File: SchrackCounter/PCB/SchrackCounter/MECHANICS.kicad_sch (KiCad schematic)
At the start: 24 parts, among them J3 Conn_01x02_Pin, J4 Conn_01x02_Pin, J5 MEM2067-02-180-00-A_REVB, M1 Fan_CPU_4pin, SW1 SW_Push, SW2 SW_Push, SW3 SW_Push, SW4 SW_Push

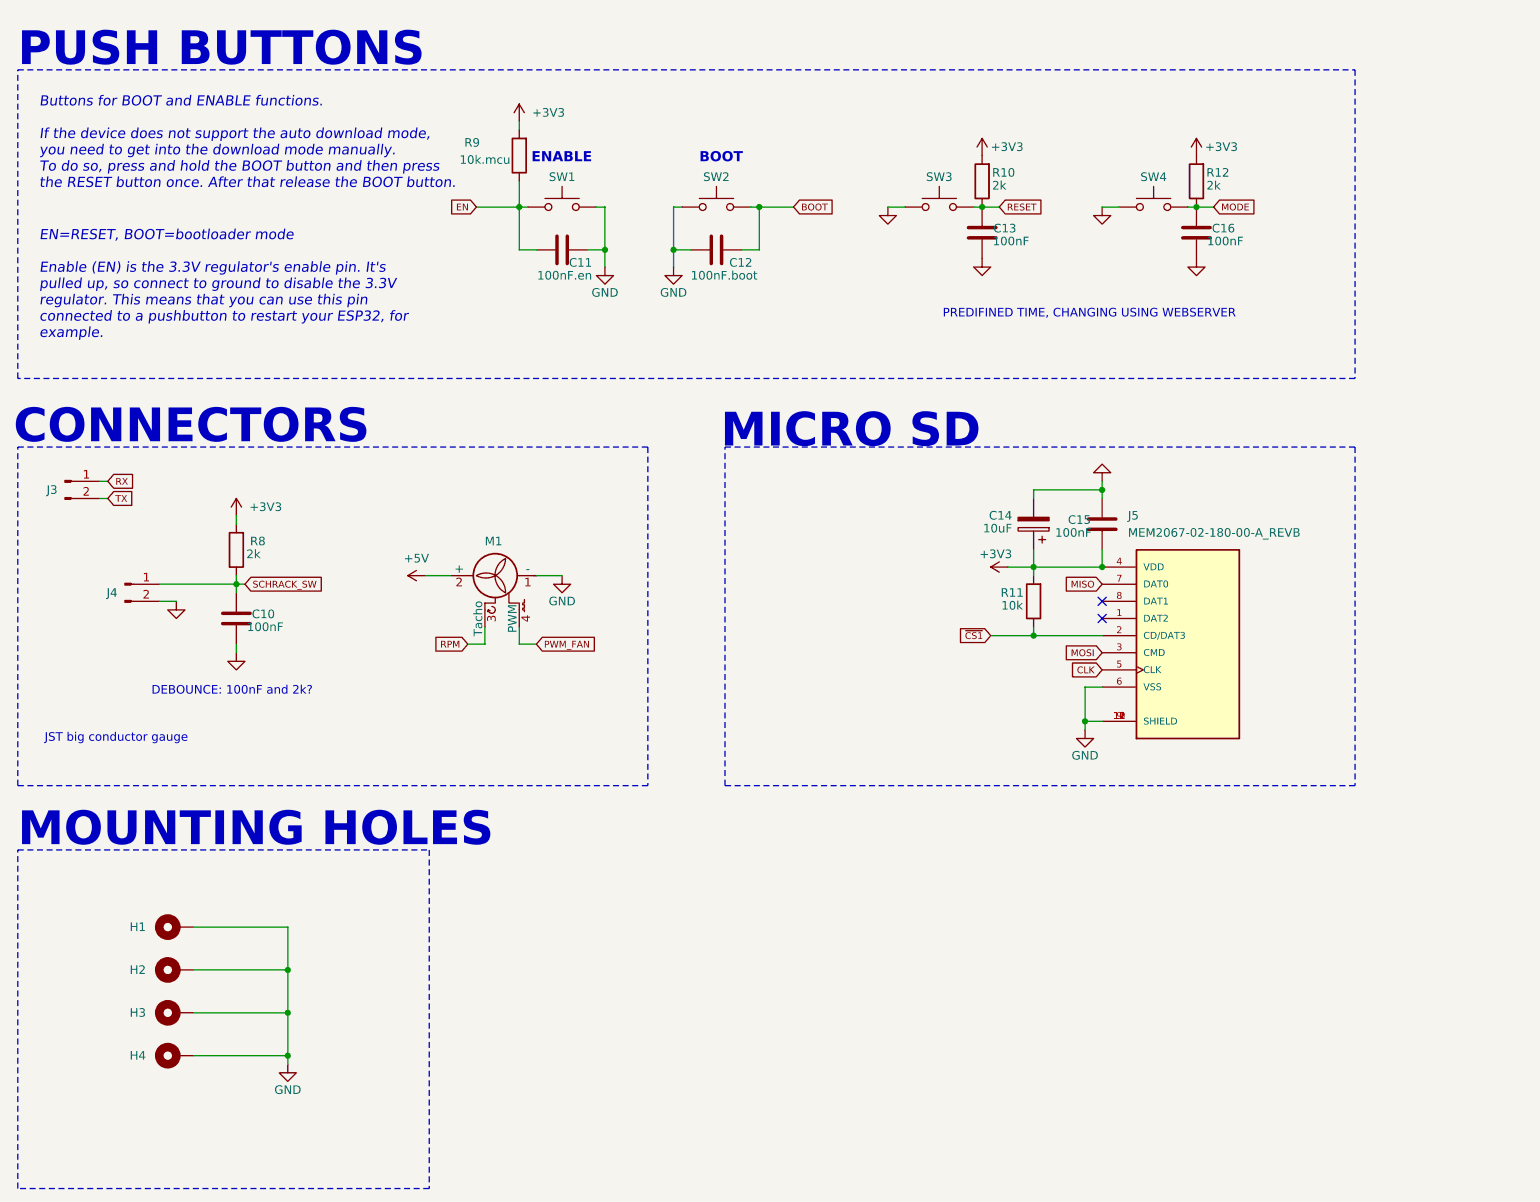
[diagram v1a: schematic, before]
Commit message: PCB Layout update
finished layout for the PCB will check for errors tommorow
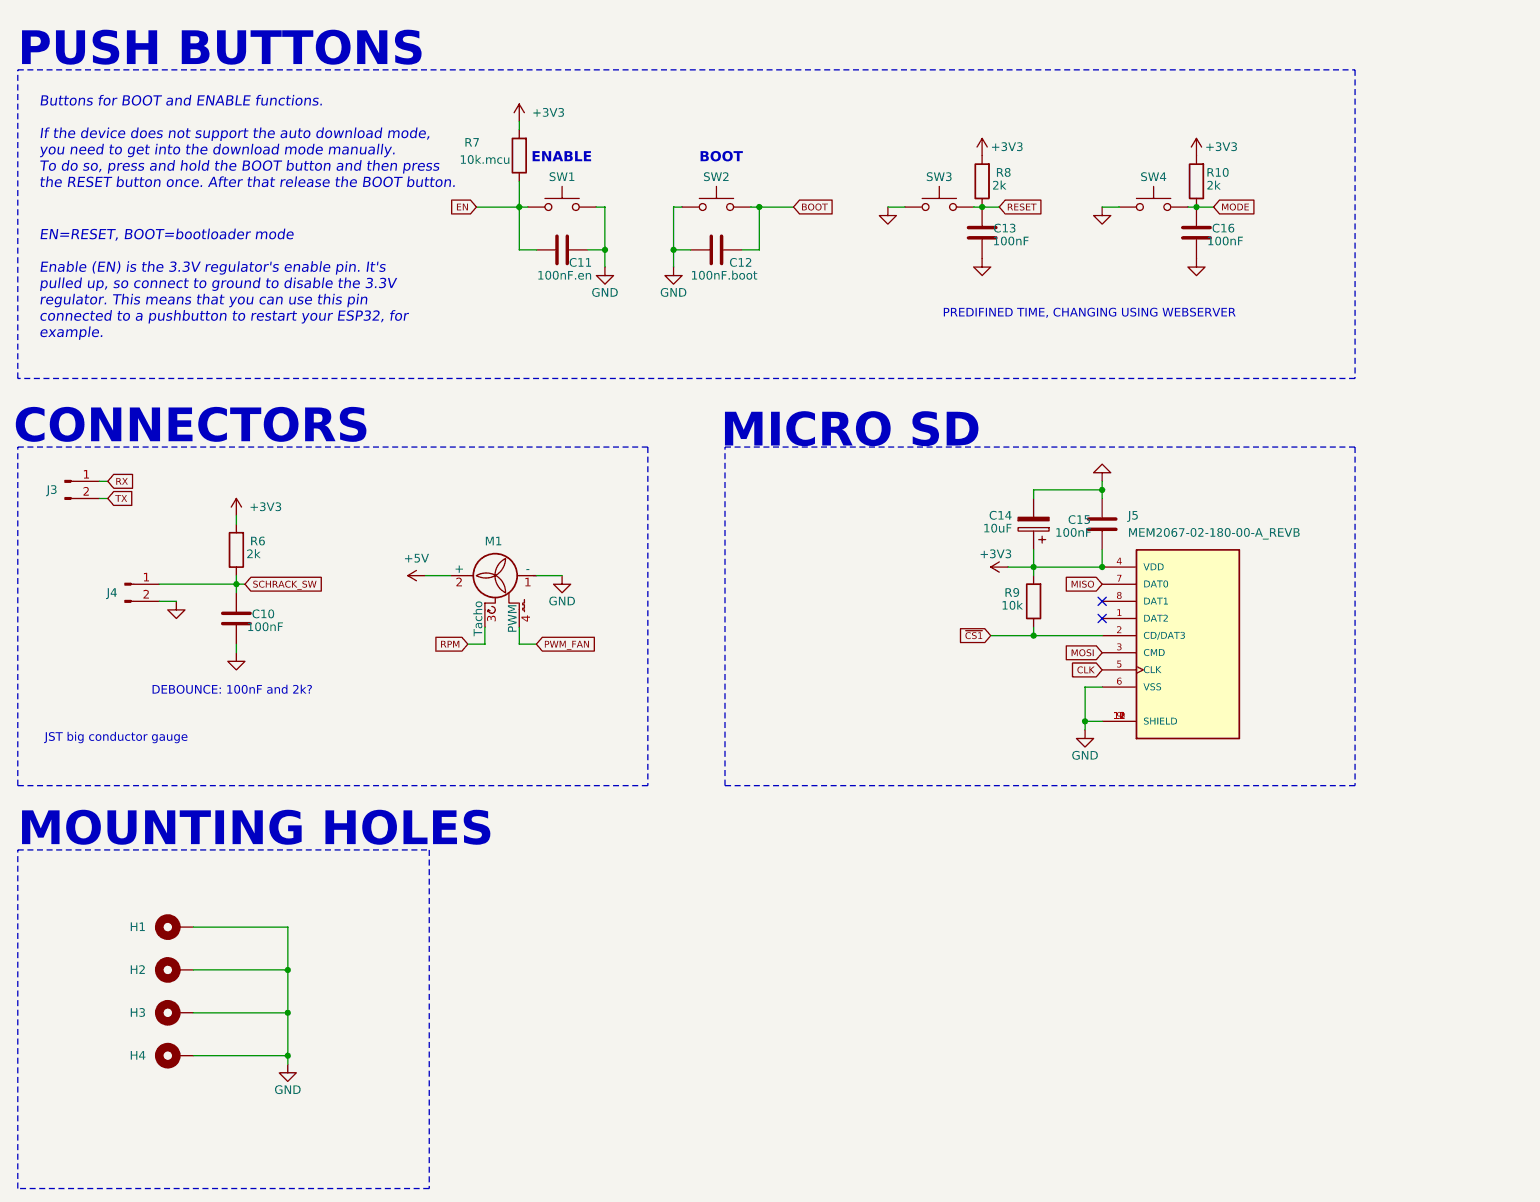
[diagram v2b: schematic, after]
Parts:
- renumbered R12 to R10, R8 to R6, R9 to R7, R10 to R8, R11 to R9
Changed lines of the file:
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@@
 		(on_board yes)
 		(dnp no)
-		(property "Reference" "R8"
+		(property "Reference" "R6"
 			(at 75.565 95.25 0)
 			(effects
@@
 			(project "SchrackCounter"
 				(path "/d96f2ffc-3f4c-4f71-b693-29f6b8c3245d/0ccd8f36-c6f2-454f-91e2-c1976b699e0e"
-					(reference "R8")
+					(reference "R6")
 					(unit 1)
 				)
@@
 		(on_board yes)
 		(dnp no)
-		(property "Reference" "R10"
+		(property "Reference" "R8"
 			(at 186.055 40.64 0)
 			(effects
@@
 			(project "SchrackCounter"
 				(path "/d96f2ffc-3f4c-4f71-b693-29f6b8c3245d/0ccd8f36-c6f2-454f-91e2-c1976b699e0e"
-					(reference "R10")
+					(reference "R8")
 					(unit 1)
 				)
@@
 		(on_board yes)
 		(dnp no)
-		(property "Reference" "R9"
+		(property "Reference" "R7"
 			(at 107.315 36.195 0)
 			(effects
@@
 			(project "SchrackCounter"
 				(path "/d96f2ffc-3f4c-4f71-b693-29f6b8c3245d/0ccd8f36-c6f2-454f-91e2-c1976b699e0e"
-					(reference "R9")
+					(reference "R7")
 					(unit 1)
 				)
@@
 		(on_board yes)
 		(dnp no)
-		(property "Reference" "R12"
+		(property "Reference" "R10"
 			(at 217.805 40.64 0)
 			(effects
@@
 			(project "SchrackCounter"
 				(path "/d96f2ffc-3f4c-4f71-b693-29f6b8c3245d/0ccd8f36-c6f2-454f-91e2-c1976b699e0e"
-					(reference "R12")
+					(reference "R10")
 					(unit 1)
 				)
@@
 		(on_board yes)
 		(dnp no)
-		(property "Reference" "R11"
+		(property "Reference" "R9"
 			(at 187.325 102.87 0)
 			(effects
@@
 			(project "SchrackCounter"
 				(path "/d96f2ffc-3f4c-4f71-b693-29f6b8c3245d/0ccd8f36-c6f2-454f-91e2-c1976b699e0e"
-					(reference "R11")
-					(unit 1)
-				)
+					(reference "R9")
+					(unit 1)
+				)

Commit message: PCB layout update
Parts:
- removed J3: Conn_01x02_Pin, Connector_PinHeader_2.54mm:PinHeader_1x02_P2.54mm_Vertical, symbol Connector:Conn_01x02_Pin
- removed J4: Conn_01x02_Pin, Connector_JST:JST_XH_B2B-XH-A_1x02_P2.50mm_Vertical, symbol Connector:Conn_01x02_Pin
- removed M1: Fan_CPU_4pin, Connector:FanPinHeader_1x04_P2.54mm_Vertical, symbol Motor:Fan_CPU_4pin
- added SW3: SW_Push, Connector_JST:JST_XH_B2B-XH-A_1x02_P2.50mm_Vertical, symbol Switch:SW_Push
- renumbered C13 to C10, C16 to C11, C10 to C12, C11 to C13, C12 to C14, C14 to C15, C15 to C16, J5 to J3, R8 to R10, R10 to R11, R7 to R12, R6 to R13, R9 to R14, SW3 to SW1, SW4 to SW2, SW1 to SW4, SW2 to SW5
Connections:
- net GND: now also SW3.1
- net SCHRACK_SW: now also SW3.2
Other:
- moved on the sheet: C10, C11, C12, C13, C14, C15, C16, H1, H2, H3, H4, J3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

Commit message: SchrackCounter
PCB Finished
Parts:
- renumbered C11 to C10, C12 to C11, C13 to C12, C10 to C13, R11 to R10, R13 to R11, R10 to R13, SW2 to SW1, SW3 to SW2, SW1 to SW3
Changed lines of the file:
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@@
 		(on_board yes)
 		(dnp no)
-		(property "Reference" "#PWR035"
+		(property "Reference" "#PWR033"
 			(at 114.3 39.37 0)
 			(effects
@@
 			(project "SchrackCounter"
 				(path "/d96f2ffc-3f4c-4f71-b693-29f6b8c3245d/0ccd8f36-c6f2-454f-91e2-c1976b699e0e"
-					(reference "#PWR035")
+					(reference "#PWR033")
 					(unit 1)
 				)
@@
 		(on_board yes)
 		(dnp no)
-		(property "Reference" "#PWR033"
+		(property "Reference" "#PWR028"
 			(at 64.77 118.11 0)
 			(effects
@@
 			(project "SchrackCounter"
 				(path "/d96f2ffc-3f4c-4f71-b693-29f6b8c3245d/0ccd8f36-c6f2-454f-91e2-c1976b699e0e"
-					(reference "#PWR033")
+					(reference "#PWR028")
 					(unit 1)
 				)
@@
 		(on_board yes)
 		(dnp no)
-		(property "Reference" "#PWR041"
+		(property "Reference" "#PWR040"
 			(at 223.52 129.54 0)
 			(effects
@@
 			(project "SchrackCounter"
 				(path "/d96f2ffc-3f4c-4f71-b693-29f6b8c3245d/0ccd8f36-c6f2-454f-91e2-c1976b699e0e"
-					(reference "#PWR041")
+					(reference "#PWR040")
 					(unit 1)
 				)
@@
 		(on_board yes)
 		(dnp no)
-		(property "Reference" "#PWR040"
+		(property "Reference" "#PWR038"
 			(at 215.9 99.06 0)
 			(effects
@@
 			(project "SchrackCounter"
 				(path "/d96f2ffc-3f4c-4f71-b693-29f6b8c3245d/0ccd8f36-c6f2-454f-91e2-c1976b699e0e"
-					(reference "#PWR040")
+					(reference "#PWR038")
 					(unit 1)
 				)
@@
 		(on_board yes)
 		(dnp no)
-		(property "Reference" "R13"
+		(property "Reference" "R11"
 			(at 95.885 99.06 0)
 			(effects
@@
 			(project "SchrackCounter"
 				(path "/d96f2ffc-3f4c-4f71-b693-29f6b8c3245d/0ccd8f36-c6f2-454f-91e2-c1976b699e0e"
-					(reference "R13")
+					(reference "R11")
 					(unit 1)
 				)
@@
 		(on_board yes)
 		(dnp no)
-		(property "Reference" "R10"
+		(property "Reference" "R13"
 			(at 127.635 99.06 0)
 			(effects
@@
 			(project "SchrackCounter"
 				(path "/d96f2ffc-3f4c-4f71-b693-29f6b8c3245d/0ccd8f36-c6f2-454f-91e2-c1976b699e0e"
-					(reference "R10")
+					(reference "R13")
 					(unit 1)
 				)
@@
 		(on_board yes)
 		(dnp no)
-		(property "Reference" "#PWR039"
+		(property "Reference" "#PWR037"
 			(at 137.16 63.5 0)
 			(effects
@@
 			(project "SchrackCounter"
 				(path "/d96f2ffc-3f4c-4f71-b693-29f6b8c3245d/0ccd8f36-c6f2-454f-91e2-c1976b699e0e"
-					(reference "#PWR039")
+					(reference "#PWR037")
 					(unit 1)
 				)
@@
 		(on_board yes)
 		(dnp no)
-		(property "Reference" "SW1"
+		(property "Reference" "SW3"
 			(at 118.11 99.695 0)
 			(effects
@@
 			(project "SchrackCounter"
 				(path "/d96f2ffc-3f4c-4f71-b693-29f6b8c3245d/0ccd8f36-c6f2-454f-91e2-c1976b699e0e"
-					(reference "SW1")
+					(reference "SW3")
 					(unit 1)
 				)
@@
 		(on_board yes)
 		(dnp no)
-		(property "Reference" "#PWR038"
+		(property "Reference" "#PWR036"
 			(at 127 63.5 0)
 			(effects
@@
 			(project "SchrackCounter"
 				(path "/d96f2ffc-3f4c-4f71-b693-29f6b8c3245d/0ccd8f36-c6f2-454f-91e2-c1976b699e0e"
-					(reference "#PWR038")
+					(reference "#PWR036")
 					(unit 1)
 				)
@@
 		(on_board yes)
 		(dnp no)
-		(property "Reference" "#PWR030"
+		(property "Reference" "#PWR026"
 			(at 50.8 110.49 0)
 			(effects
@@
 			(project "SchrackCounter"
 				(path "/d96f2ffc-3f4c-4f71-b693-29f6b8c3245d/0ccd8f36-c6f2-454f-91e2-c1976b699e0e"
-					(reference "#PWR030")
+					(reference "#PWR026")
 					(unit 1)
 				)
@@
 		(on_board yes)
 		(dnp no)
-		(property "Reference" "#PWR036"
+		(property "Reference" "#PWR030"
 			(at 92.71 100.33 0)
 			(effects
@@
 			(project "SchrackCounter"
 				(path "/d96f2ffc-3f4c-4f71-b693-29f6b8c3245d/0ccd8f36-c6f2-454f-91e2-c1976b699e0e"
-					(reference "#PWR036")
+					(reference "#PWR030")
 					(unit 1)
 				)
@@
 		(on_board yes)
 		(dnp no)
-		(property "Reference" "C10"
+		(property "Reference" "C13"
 			(at 129.54 107.315 0)
 			(effects
@@
 			(project "SchrackCounter"
 				(path "/d96f2ffc-3f4c-4f71-b693-29f6b8c3245d/0ccd8f36-c6f2-454f-91e2-c1976b699e0e"
-					(reference "C10")
+					(reference "C13")
 					(unit 1)
 				)
@@
 		(on_board yes)
 		(dnp no)
-		(property "Reference" "#PWR037"
+		(property "Reference" "#PWR031"
 			(at 92.71 118.11 0)
 			(effects
@@
 			(project "SchrackCounter"
 				(path "/d96f2ffc-3f4c-4f71-b693-29f6b8c3245d/0ccd8f36-c6f2-454f-91e2-c1976b699e0e"
-					(reference "#PWR037")
+					(reference "#PWR031")
 					(unit 1)
 				)
@@
 		(on_board yes)
 		(dnp no)
-		(property "Reference" "#PWR034"
+		(property "Reference" "#PWR029"
 			(at 78.74 110.49 0)
 			(effects
@@
 			(project "SchrackCounter"
 				(path "/d96f2ffc-3f4c-4f71-b693-29f6b8c3245d/0ccd8f36-c6f2-454f-91e2-c1976b699e0e"
-					(reference "#PWR034")
+					(reference "#PWR029")
 					(unit 1)
 				)
@@
 		(on_board yes)
 		(dnp no)
-		(property "Reference" "#PWR029"
+		(property "Reference" "#PWR035"
 			(at 124.46 118.11 0)
 			(effects
@@
 			(project "SchrackCounter"
 				(path "/d96f2ffc-3f4c-4f71-b693-29f6b8c3245d/0ccd8f36-c6f2-454f-91e2-c1976b699e0e"
-					(reference "#PWR029")
+					(reference "#PWR035")
 					(unit 1)
 				)
@@
 		(on_board yes)
 		(dnp no)
-		(property "Reference" "SW3"
+		(property "Reference" "SW2"
 			(at 86.36 99.695 0)
 			(effects
@@
 			(project "SchrackCounter"
 				(path "/d96f2ffc-3f4c-4f71-b693-29f6b8c3245d/0ccd8f36-c6f2-454f-91e2-c1976b699e0e"
-					(reference "SW3")
+					(reference "SW2")
 					(unit 1)
 				)
@@
 		(on_board yes)
 		(dnp no)
-		(property "Reference" "#PWR042"
+		(property "Reference" "#PWR041"
 			(at 226.06 80.01 0)
 			(effects
@@
 			(project "SchrackCounter"
 				(path "/d96f2ffc-3f4c-4f71-b693-29f6b8c3245d/0ccd8f36-c6f2-454f-91e2-c1976b699e0e"
-					(reference "#PWR042")
+					(reference "#PWR041")
 					(unit 1)
 				)
@@
 		(on_board yes)
 		(dnp no)
-		(property "Reference" "#PWR031"
+		(property "Reference" "#PWR039"
 			(at 218.44 62.23 0)
 			(effects
@@
 			(project "SchrackCounter"
 				(path "/d96f2ffc-3f4c-4f71-b693-29f6b8c3245d/0ccd8f36-c6f2-454f-91e2-c1976b699e0e"
-					(reference "#PWR031")
+					(reference "#PWR039")
 					(unit 1)
 				)
@@
 		(on_board yes)
 		(dnp no)
-		(property "Reference" "R11"
+		(property "Reference" "R10"
 			(at 67.945 99.06 0)
 			(effects
@@
 			(project "SchrackCounter"
 				(path "/d96f2ffc-3f4c-4f71-b693-29f6b8c3245d/0ccd8f36-c6f2-454f-91e2-c1976b699e0e"
-					(reference "R11")
+					(reference "R10")
 					(unit 1)
 				)
@@
 		(on_board yes)
 		(dnp no)
-		(property "Reference" "#PWR028"
+		(property "Reference" "#PWR034"
 			(at 124.46 100.33 0)
 			(effects
@@
 			(project "SchrackCounter"
 				(path "/d96f2ffc-3f4c-4f71-b693-29f6b8c3245d/0ccd8f36-c6f2-454f-91e2-c1976b699e0e"
-					(reference "#PWR028")
+					(reference "#PWR034")
 					(unit 1)
 				)
@@
 		(on_board yes)
 		(dnp no)
-		(property "Reference" "C11"
+		(property "Reference" "C10"
 			(at 69.85 107.315 0)
 			(effects
@@
 			(project "SchrackCounter"
 				(path "/d96f2ffc-3f4c-4f71-b693-29f6b8c3245d/0ccd8f36-c6f2-454f-91e2-c1976b699e0e"
-					(reference "C11")
+					(reference "C10")
 					(unit 1)
 				)
@@
 		(on_board yes)
 		(dnp no)
-		(property "Reference" "#PWR027"
+		(property "Reference" "#PWR032"
 			(at 110.49 110.49 0)
 			(effects
@@
 			(project "SchrackCounter"
 				(path "/d96f2ffc-3f4c-4f71-b693-29f6b8c3245d/0ccd8f36-c6f2-454f-91e2-c1976b699e0e"
-					(reference "#PWR027")
+					(reference "#PWR032")
 					(unit 1)
 				)
@@
 		(on_board yes)
 		(dnp no)
-		(property "Reference" "SW2"
+		(property "Reference" "SW1"
 			(at 58.42 99.695 0)
 			(effects
@@
 			(project "SchrackCounter"
 				(path "/d96f2ffc-3f4c-4f71-b693-29f6b8c3245d/0ccd8f36-c6f2-454f-91e2-c1976b699e0e"
-					(reference "SW2")
+					(reference "SW1")
 					(unit 1)
 				)
@@
 		(on_board yes)
 		(dnp no)
-		(property "Reference" "#PWR032"
+		(property "Reference" "#PWR027"
 			(at 64.77 100.33 0)
 			(effects
@@
 			(project "SchrackCounter"
 				(path "/d96f2ffc-3f4c-4f71-b693-29f6b8c3245d/0ccd8f36-c6f2-454f-91e2-c1976b699e0e"
-					(reference "#PWR032")
+					(reference "#PWR027")
 					(unit 1)
 				)
@@
 		(on_board yes)
 		(dnp no)
-		(property "Reference" "C13"
+		(property "Reference" "C12"
 			(at 125.095 56.515 90)
 			(effects
@@
 			(project "SchrackCounter"
 				(path "/d96f2ffc-3f4c-4f71-b693-29f6b8c3245d/0ccd8f36-c6f2-454f-91e2-c1976b699e0e"
-					(reference "C13")
+					(reference "C12")
 					(unit 1)
 				)
@@
 		(on_board yes)
 		(dnp no)
-		(property "Reference" "C12"
+		(property "Reference" "C11"
 			(at 97.79 107.315 0)
 			(effects
@@
 			(project "SchrackCounter"
 				(path "/d96f2ffc-3f4c-4f71-b693-29f6b8c3245d/0ccd8f36-c6f2-454f-91e2-c1976b699e0e"
-					(reference "C12")
-					(unit 1)
-				)
+					(reference "C11")
+					(unit 1)
+				)
